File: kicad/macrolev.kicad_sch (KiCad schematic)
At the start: 102 parts, among them J2 I2C, J3 DEBUG, J4 USBC, SW1 BOOT_BTN, SW2 RST_BTN, U1 A1101ELHL, U10 A1101ELHL, U11 A1101ELHL, U12 A1101ELHL, U13 A1101ELHL, U14 A1101ELHL, U15 A1101ELHL, U16 A1101ELHL, U17 A1101ELHL, U18 A1101ELHL, U19 A1101ELHL, U2 A1101ELHL, U20 A1101ELHL, U21 A1101ELHL, U22 A1101ELHL, U23 A1101ELHL, U24 A1101ELHL, U25 A1101ELHL, U26 A1101ELHL, U27 A1101ELHL, U28 A1101ELHL, U29 A1101ELHL, U3 A1101ELHL, U30 A1101ELHL, U31 A1101ELHL, U32 A1101ELHL, U33 A1101ELHL, U34 A1101ELHL, U35 A1101ELHL, U36 A1101ELHL, U37 A1101ELHL, U38 A1101ELHL, U39 A1101ELHL, U4 A1101ELHL, U40 A1101ELHL, U41 A1101ELHL, U42 A1101ELHL, U43 A1101ELHL, U44 A1101ELHL, U45 A1101ELHL, U46 A1101ELHL, U47 A1101ELHL, U48 A1101ELHL, U49 A1101ELHL, U5 A1101ELHL, U50 A1101ELHL, U51 A1101ELHL, U52 A1101ELHL, U53 A1101ELHL, U54 A1101ELHL, U55 A1101ELHL, U56 A1101ELHL, U57 A1101ELHL, U58 A1101ELHL, U59 A1101ELHL, U6 A1101ELHL, U60 A1101ELHL, U61 A1101ELHL, U62 A1101ELHL, U63 A1101ELHL, U64 A1101ELHL, U65 A1101ELHL, U66 A1101ELHL, U67 A1101ELHL, U68 AMS1117-3.3, U69 STM32F411CEU6, U7 A1101ELHL, U8 A1101ELHL, U9 A1101ELHL, Y1 25MHz/20ppm/15pF

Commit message: fix(pcb): apply feedback from PrintedCircuitBoard sub
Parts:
- removed J2: I2C, Connector_PinHeader_2.54mm:PinHeader_1x04_P2.54mm_Vertical, symbol Connector:Conn_01x04_Pin
- removed J3: DEBUG, Connector_PinHeader_2.54mm:PinHeader_1x04_P2.54mm_Vertical, symbol Connector:Conn_01x04_Pin
- removed J4: USBC, Connector_PinHeader_2.54mm:PinHeader_1x04_P2.54mm_Vertical, symbol Connector:Conn_01x04_Pin
- added J1: USBC, Connector_PinHeader_2.54mm:PinHeader_1x04_P2.54mm_Vertical, symbol Connector_Generic:Conn_01x04
- added J2: I2C, Connector_PinHeader_2.54mm:PinHeader_1x04_P2.54mm_Vertical, symbol Connector_Generic:Conn_01x04
- added J3: DEBUG, Connector_PinHeader_2.54mm:PinHeader_1x04_P2.54mm_Vertical, symbol Connector_Generic:Conn_01x04
- added R1, R2: 1.2K, Resistor_SMD:R_0402_1005Metric_Pad0.72x0.64mm_HandSolder, symbol Device:R
- SW1: value BOOT_BTN -> RST_BTN
- SW2: value RST_BTN -> BOOT_BTN
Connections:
- net +3.3V: now also J2.4 (Pin_4), J3.4 (Pin_4), R1.1, R2.1
- net GND: now also J1.1 (Pin_1), J2.1 (Pin_1), J3.1 (Pin_1)
- net I2C_SCL: now also J2.3 (Pin_3), R1.2
- net I2C_SDA: now also J2.2 (Pin_2), R2.2
- net SWCLK: now also J3.2 (Pin_2)
- net SWDIO: now also J3.3 (Pin_3)
- net USB_D+: now also J1.4 (Pin_4)
- net USB_D-: now also J1.3 (Pin_3)
- net VBUS: now also J1.2 (Pin_2)
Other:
- note removed: "Connectors"
- moved on the sheet: C1, C10, C11, C12, C13, C2, C3, C4, C5, C6, C7, C8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

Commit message: change pcb routing
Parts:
- C1: LCSC (none) -> C19702
- C10, C11: LCSC (none) -> C45783
- C12, C13: LCSC (none) -> C1554
- C2, C3, C4, C5, C9: LCSC (none) -> C1525
- C6: LCSC (none) -> C15195
- C7, C8: LCSC (none) -> C52923
- D1: LCSC (none) -> C2286
- FB1, FB2: LCSC (none) -> C76892
- R1, R2: LCSC (none) -> C25862
- R3, R4: LCSC (none) -> C25744
- R5: LCSC (none) -> C25905
- SW1, SW2: JLCPCB part  C139797 -> (none); LCSC (none) -> C139797
- U1, U10, U11, U12, U13, U14, U15, U16, U17, U18, U19, U2, U20, U21, U22, U23, U24, U25, U26, U27, U28, U29, U3, U30, U31, U32, U33, U34, U35, U36, U37, U38, U39, U4, U40, U41, U42, U43, U44, U45, U46, U47, U48, U49, U5, U50, U51, U52, U53, U54, U55, U56, U57, U58, U59, U6, U60, U61, U62, U63, U64, U65, U66, U67, U7, U8, U9: LCSC (none) -> C266230
- U68: LCSC (none) -> C6186
- U69: LCSC (none) -> C60420
- Y1: JLCPCB part  C382475 -> (none); LCSC (none) -> C387396

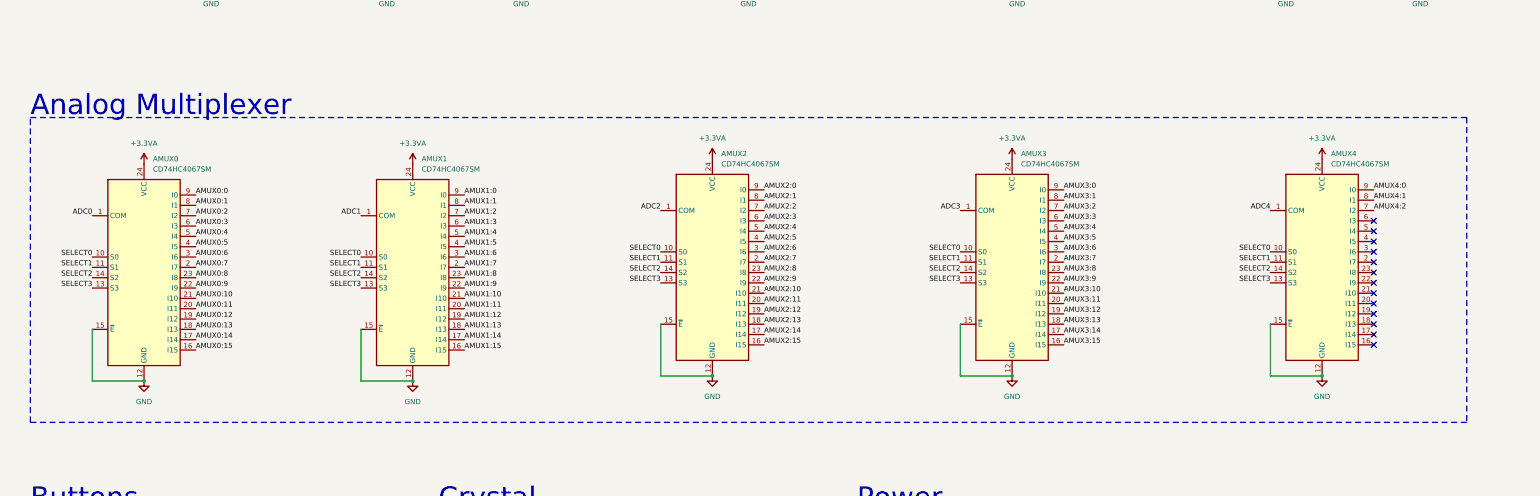
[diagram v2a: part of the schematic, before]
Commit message: add caps on amux, change routing
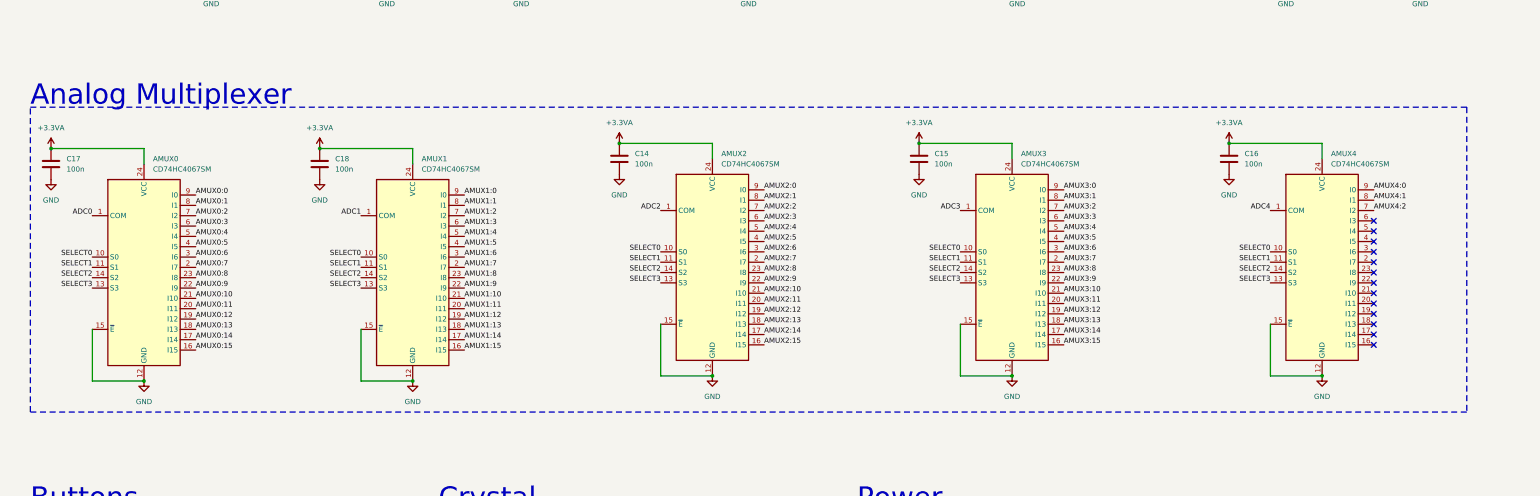
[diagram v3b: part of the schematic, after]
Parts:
- added C14, C15, C16, C17, C18: 100n, Capacitor_SMD:C_0402_1005Metric_Pad0.74x0.62mm_HandSolder, symbol Device:C
- AMUX0, AMUX1, AMUX2, AMUX3, AMUX4: LCSC C98457 -> C179326
- U1, U10, U11, U12, U13, U14, U16, U18, U19, U2, U20, U21, U22, U23, U24, U25, U26, U27, U28, U29, U3, U31, U33, U34, U35, U36, U37, U38, U39, U4, U40, U41, U42, U43, U44, U46, U47, U48, U49, U5, U50, U51, U52, U53, U54, U55, U56, U6, U64, U65, U66, U67, U7, U8, U9: footprint Lekker switch:SW_MX_Lekker_1u -> Package_TO_SOT_SMD:SOT-23
- U15, U30, U57, U61, U62: footprint Lekker switch:SW_MX_Lekker -> Package_TO_SOT_SMD:SOT-23
- U17: footprint Lekker switch:SW_MX_Lekker_1.5u -> Package_TO_SOT_SMD:SOT-23
- U32, U58: footprint Lekker switch:SW_MX_Lekker_1.75u -> Package_TO_SOT_SMD:SOT-23
- U45, U59, U60, U63: footprint Lekker switch:SW_MX_Lekker_1.25u -> Package_TO_SOT_SMD:SOT-23
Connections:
- net +3.3VA: now also C14.1, C15.1, C16.1, C17.1, C18.1
- net GND: now also C14.2, C15.2, C16.2, C17.2, C18.2

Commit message: wip: fix pcb
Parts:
- removed SW1: RST_BTN, switch:SKRPACE010, symbol Switch:SW_Push_Dual
- removed SW2: BOOT_BTN, switch:SKRPACE010, symbol Switch:SW_Push_Dual
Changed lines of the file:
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@@
   (junction (at 483.87 257.81) (diameter 0) (color 0 0 0 0)
   )
-  (junction (at 73.66 341.63) (diameter 0) (color 0 0 0 0)
-  )
   (junction (at 481.33 257.81) (diameter 0) (color 0 0 0 0)
   )
@@
   (junction (at 149.86 367.03) (diameter 0) (color 0 0 0 0)
   )
-  (junction (at 60.96 341.63) (diameter 0) (color 0 0 0 0)
-  )
   (junction (at 450.85 254) (diameter 0) (color 0 0 0 0)
   )
@@
   (junction (at 547.37 243.84) (diameter 0) (color 0 0 0 0)
   )
-  (junction (at 53.34 372.11) (diameter 0) (color 0 0 0 0)
-  )
   (junction (at 491.49 243.84) (diameter 0) (color 0 0 0 0)
   )
-  (junction (at 73.66 372.11) (diameter 0) (color 0 0 0 0)
-  )
   (junction (at 293.37 354.33) (diameter 0) (color 0 0 0 0)
   )
@@
   (junction (at 483.87 341.63) (diameter 0) (color 0 0 0 0)
   )
-  (junction (at 73.66 354.33) (diameter 0) (color 0 0 0 0)
-  )
   (junction (at 520.7 254) (diameter 0) (color 0 0 0 0)
   )
@@
   (junction (at 425.45 254) (diameter 0) (color 0 0 0 0)
   )
-  (junction (at 60.96 342.9) (diameter 0) (color 0 0 0 0)
-  )
   (junction (at 438.15 254) (diameter 0) (color 0 0 0 0)
   )
-  (junction (at 63.5 372.11) (diameter 0) (color 0 0 0 0)
-  )
   (junction (at 116.84 289.56) (diameter 0) (color 0 0 0 0)
   )
@@
   (junction (at 447.04 290.83) (diameter 0) (color 0 0 0 0)
   )
-  (junction (at 60.96 353.06) (diameter 0) (color 0 0 0 0)
-  )
   (junction (at 167.64 231.14) (diameter 0) (color 0 0 0 0)
   )
+  (junction (at 73.66 341.63) (diameter 0) (color 0 0 0 0)
+  )
   (junction (at 520.7 243.84) (diameter 0) (color 0 0 0 0)
   )
@@
     (stroke (width 0) (type default))
   )
-  (wire (pts (xy 60.96 353.06) (xy 60.96 354.33))
-    (stroke (width 0) (type default))
-  )
   (wire (pts (xy 320.04 353.06) (xy 320.04 354.33))
     (stroke (width 0) (type default))
@@
     (stroke (width 0) (type default))
   )
-  (wire (pts (xy 60.96 353.06) (xy 66.04 353.06))
-    (stroke (width 0) (type default))
-  )
   (wire (pts (xy 412.75 252.73) (xy 412.75 254))
     (stroke (width 0) (type default))
@@
     (stroke (width 0) (type default))
   )
-  (wire (pts (xy 60.96 341.63) (xy 60.96 342.9))
-    (stroke (width 0) (type default))
-  )
   (wire (pts (xy 486.41 257.81) (xy 486.41 259.08))
     (stroke (width 0) (type default))
@@
     (stroke (width 0) (type default))
   )
-  (wire (pts (xy 53.34 372.11) (xy 53.34 377.19))
-    (stroke (width 0) (type default))
-  )
   (wire (pts (xy 138.43 353.06) (xy 146.05 353.06))
     (stroke (width 0) (type default))
@@
     (stroke (width 0) (type default))
   )
-  (wire (pts (xy 463.55 254) (xy 450.85 254))
+  (wire (pts (xy 54.61 341.63) (xy 73.66 341.63))
     (stroke (width 0) (type default))
   )
-  (wire (pts (xy 63.5 372.11) (xy 73.66 372.11))
+  (wire (pts (xy 463.55 254) (xy 450.85 254))
     (stroke (width 0) (type default))
   )
@@
     (stroke (width 0) (type default))
   )
-  (wire (pts (xy 60.96 354.33) (xy 73.66 354.33))
-    (stroke (width 0) (type default))
-  )
   (wire (pts (xy 505.46 252.73) (xy 505.46 254))
     (stroke (width 0) (type default))
@@
     (stroke (width 0) (type default))
   )
-  (wire (pts (xy 60.96 342.9) (xy 66.04 342.9))
-    (stroke (width 0) (type default))
-  )
   (wire (pts (xy 486.41 257.81) (xy 483.87 257.81))
     (stroke (width 0) (type default))
@@
     (stroke (width 0) (type default))
   )
-  (wire (pts (xy 73.66 353.06) (xy 73.66 354.33))
+  (wire (pts (xy 73.66 353.06) (xy 73.66 355.6))
     (stroke (width 0) (type default))
   )
@@
     (stroke (width 0) (type default))
   )
-  (wire (pts (xy 73.66 355.6) (xy 73.66 354.33))
-    (stroke (width 0) (type default))
-  )
   (wire (pts (xy 266.7 344.17) (xy 273.05 344.17))
     (stroke (width 0) (type default))
@@
     (stroke (width 0) (type default))
   )
-  (wire (pts (xy 63.5 372.11) (xy 63.5 377.19))
-    (stroke (width 0) (type default))
-  )
   (wire (pts (xy 116.84 236.22) (xy 116.84 232.41))
     (stroke (width 0) (type default))
@@
     (stroke (width 0) (type default))
   )
-  (wire (pts (xy 60.96 341.63) (xy 73.66 341.63))
-    (stroke (width 0) (type default))
-  )
   (wire (pts (xy 190.5 234.95) (xy 190.5 231.14))
     (stroke (width 0) (type default))
@@
     (stroke (width 0) (type default))
   )
-  (wire (pts (xy 54.61 341.63) (xy 60.96 341.63))
-    (stroke (width 0) (type default))
-  )
   (wire (pts (xy 450.85 302.26) (xy 450.85 309.88))
     (stroke (width 0) (type default))
@@
     (stroke (width 0) (type default))
   )
-  (wire (pts (xy 43.18 372.11) (xy 53.34 372.11))
-    (stroke (width 0) (type default))
-  )
   (wire (pts (xy 521.97 309.88) (xy 532.13 309.88))
     (stroke (width 0) (type default))
@@
     (stroke (width 0) (type default))
   )
-  (wire (pts (xy 43.18 368.3) (xy 43.18 372.11))
-    (stroke (width 0) (type default))
-  )
   (wire (pts (xy 27.94 232.41) (xy 50.8 232.41))
     (stroke (width 0) (type default))
@@
     )
   )
-  (symbol (lib_id "Switch:SW_Push_Dual") (at 58.42 372.11 0) (mirror y) (unit 1)
-    (in_bom yes) (on_board yes) (dnp no)
-    (property "Reference" "SW2" (at 57.15 367.03 0)
-      (effects (font (size 1.27 1.27)) (justify right))
-    )
-    (property "Value" "BOOT_BTN" (at 53.34 379.73 0)
-      (effects (font (size 1.27 1.27)) (justify right))
-    )
-    (property "Footprint" "switch:SKRPACE010" (at 58.42 367.03 0)
-      (effects (font (size 1.27 1.27)) hide)
-    )
-    (property "Datasheet" "~" (at 58.42 367.03 0)
-      (effects (font (size 1.27 1.27)) hide)
-    )
-    (property "LCSC" "C139797" (at 58.42 372.11 0)
-      (effects (font (size 1.27 1.27)) hide)
-    )
-    (pin "1")
-    (pin "2")
-    (pin "3")
-    (pin "4")
-    (instances
-      (project "macrolev"
-        (path "/24af5553-bb98-43bd-b85c-c6b0b021d5e0"
-          (reference "SW2") (unit 1)
-        )
-      )
-    )
-  )
   (symbol (lib_id "Device:C") (at 450.85 248.92 0) (unit 1)
     (in_bom yes) (on_board yes) (dnp no) (fields_autoplaced)
@@
     )
   )
-  (symbol (lib_id "Switch:SW_Push_Dual") (at 60.96 347.98 90) (mirror x) (unit 1)
-    (in_bom yes) (on_board yes) (dnp no)
-    (property "Reference" "SW1" (at 52.07 346.71 90)
-      (effects (font (size 1.27 1.27)) (justify right))
-    )
-    (property "Value" "RST_BTN" (at 48.26 349.25 90)
-      (effects (font (size 1.27 1.27)) (justify right))
-    )
-    (property "Footprint" "switch:SKRPACE010" (at 55.88 347.98 0)
-      (effects (font (size 1.27 1.27)) hide)
-    )
-    (property "Datasheet" "~" (at 55.88 347.98 0)
-      (effects (font (size 1.27 1.27)) hide)
-    )
-    (property "LCSC" "C139797" (at 60.96 347.98 90)
-      (effects (font (size 1.27 1.27)) hide)
-    )
-    (pin "1")
-    (pin "2")
-    (pin "3")
-    (pin "4")
-    (instances
-      (project "macrolev"
-        (path "/24af5553-bb98-43bd-b85c-c6b0b021d5e0"
-          (reference "SW1") (unit 1)
-        )
-      )
-    )
-  )
   (symbol (lib_id "power:GND") (at 331.47 78.74 0) (unit 1)
     (in_bom yes) (on_board yes) (dnp no) (fields_autoplaced)
@@
         )
       )
-    )
-  )
-  (symbol (lib_id "power:+3.3V") (at 43.18 368.3 0) (unit 1)
-    (in_bom yes) (on_board yes) (dnp no) (fields_autoplaced)
-    (property "Reference" "#PWR0154" (at 43.18 372.11 0)
-      (effects (font (size 1.27 1.27)) hide)
-    )
-    (property "Value" "+3.3V" (at 43.18 363.22 0)
-      (effects (font (size 1.27 1.27)))
-    )
-    (property "Footprint" "" (at 43.18 368.3 0)
-      (effects (font (size 1.27 1.27)) hide)
-    )
-    (property "Datasheet" "" (at 43.18 368.3 0)
-      (effects (font (size 1.27 1.27)) hide)
-    )
-    (pin "1")
-    (instances
-      (project "macrolev"
-        (path "/24af5553-bb98-43bd-b85c-c6b0b021d5e0"
-          (reference "#PWR0154") (unit 1)
-        )
-      )

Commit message: wip rev 1.1
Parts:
- removed J1: USBC, Connector_PinHeader_2.54mm:PinHeader_1x04_P2.54mm_Vertical, symbol Connector_Generic:Conn_01x04
- removed R3: 10k, Resistor_SMD:R_0402_1005Metric_Pad0.72x0.64mm_HandSolder, symbol Device:R
- added R6, R7: 5.1K, Resistor_SMD:R_0402_1005Metric_Pad0.72x0.64mm_HandSolder, symbol Device:R
- added U70: GT-USB-7010ASV, JLCPCB:USB-C-SMD_G-SWITCH_GT-USB-7010ASV, symbol jlcpcb:GT-USB-7010ASV
- J3: footprint Connector_PinHeader_2.54mm:PinHeader_1x04_P2.54mm_Vertical -> Connector_PinHeader_2.54mm:PinHeader_1x04_P2.54mm_Horizontal
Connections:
- net GND: now also R6.2, R7.2, U70.A1B12 (GND), U70.B1A12 (GND)
- net USB_D+: now also U70.A6 (DP1), U70.B6 (DP2)
- net USB_D-: now also U70.A7 (DN1), U70.B7 (DN2)
- net VBUS: now also U70.A4B9 (VBUS), U70.B4A9 (VBUS)
- new net: R7.1, U70.B5 (CC2)
- new net: R6.1, U70.A5 (CC1)
- no-connect marks 33 -> 39
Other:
- note added: "Usb"
- moved on the sheet: C1, C2, C3, C4, C5, C6, C7, C8, FB1, J2, J3, R1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

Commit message: wip: real time key logging
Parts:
- added TP1: TestPoint, symbol Connector:TestPoint
- added U71: A1101ELHL, Package_TO_SOT_SMD:SOT-23, symbol Sensor_Magnetic:A1101ELHL
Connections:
- net +3.3VA: now also U71.1 (VCC)
- net GND: now also U71.3 (GND)
- net NRST: now also TP1.1

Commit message: wip: explore haptic feedback
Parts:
- removed TP1: TestPoint, symbol Connector:TestPoint
- removed U71: A1101ELHL, Package_TO_SOT_SMD:SOT-23, symbol Sensor_Magnetic:A1101ELHL
- added C? (x2): 1u, symbol Device:C
- added M?: Motor_DC, symbol Motor:Motor_DC
- added U?: DRV2605LDGS, Package_SO:VSSOP-10_3x3mm_P0.5mm, symbol Driver_Haptic:DRV2605LDGS
- R1, R2: value 1.2K -> 2.2K
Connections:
- net +3.3V: now also U?.5 (EN)
- net +5V: now also C?.2, U?.10 (VDD), U?.6 (VDD/NC)
- net GND: now also C?.1, C?.1, U?.4 (IN/TRIG), U?.8 (GND)
- net I2C_SCL: now also U?.2 (SCL)
- net I2C_SDA: now also U?.3 (SDA)
- new net: M?.1 (+), U?.7 (OUT+)
- new net: M?.2 (-), U?.9 (OUT-)
- new net: C?.2, U?.1 (REG)
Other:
- note added: "Motors"
- note removed: "Buttons"
- moved on the sheet: C9, R4
